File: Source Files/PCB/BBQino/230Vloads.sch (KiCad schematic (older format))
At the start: 3 parts

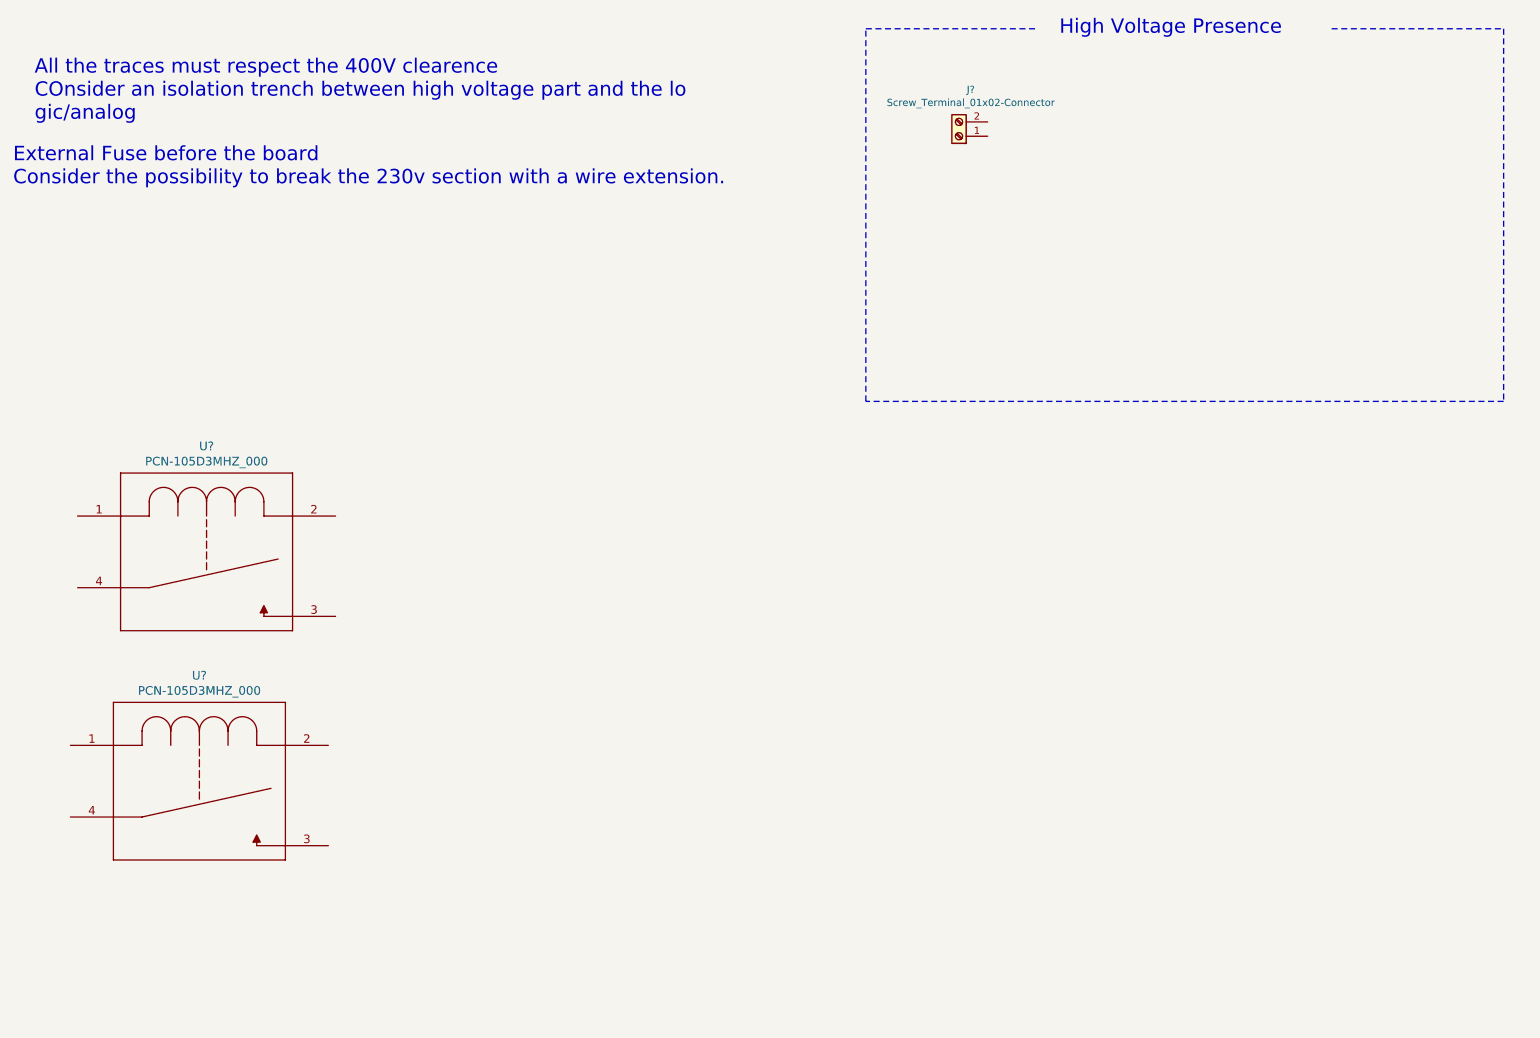
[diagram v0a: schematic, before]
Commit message: 230V section first Draft. Added external module on top of the shield for the 230V section
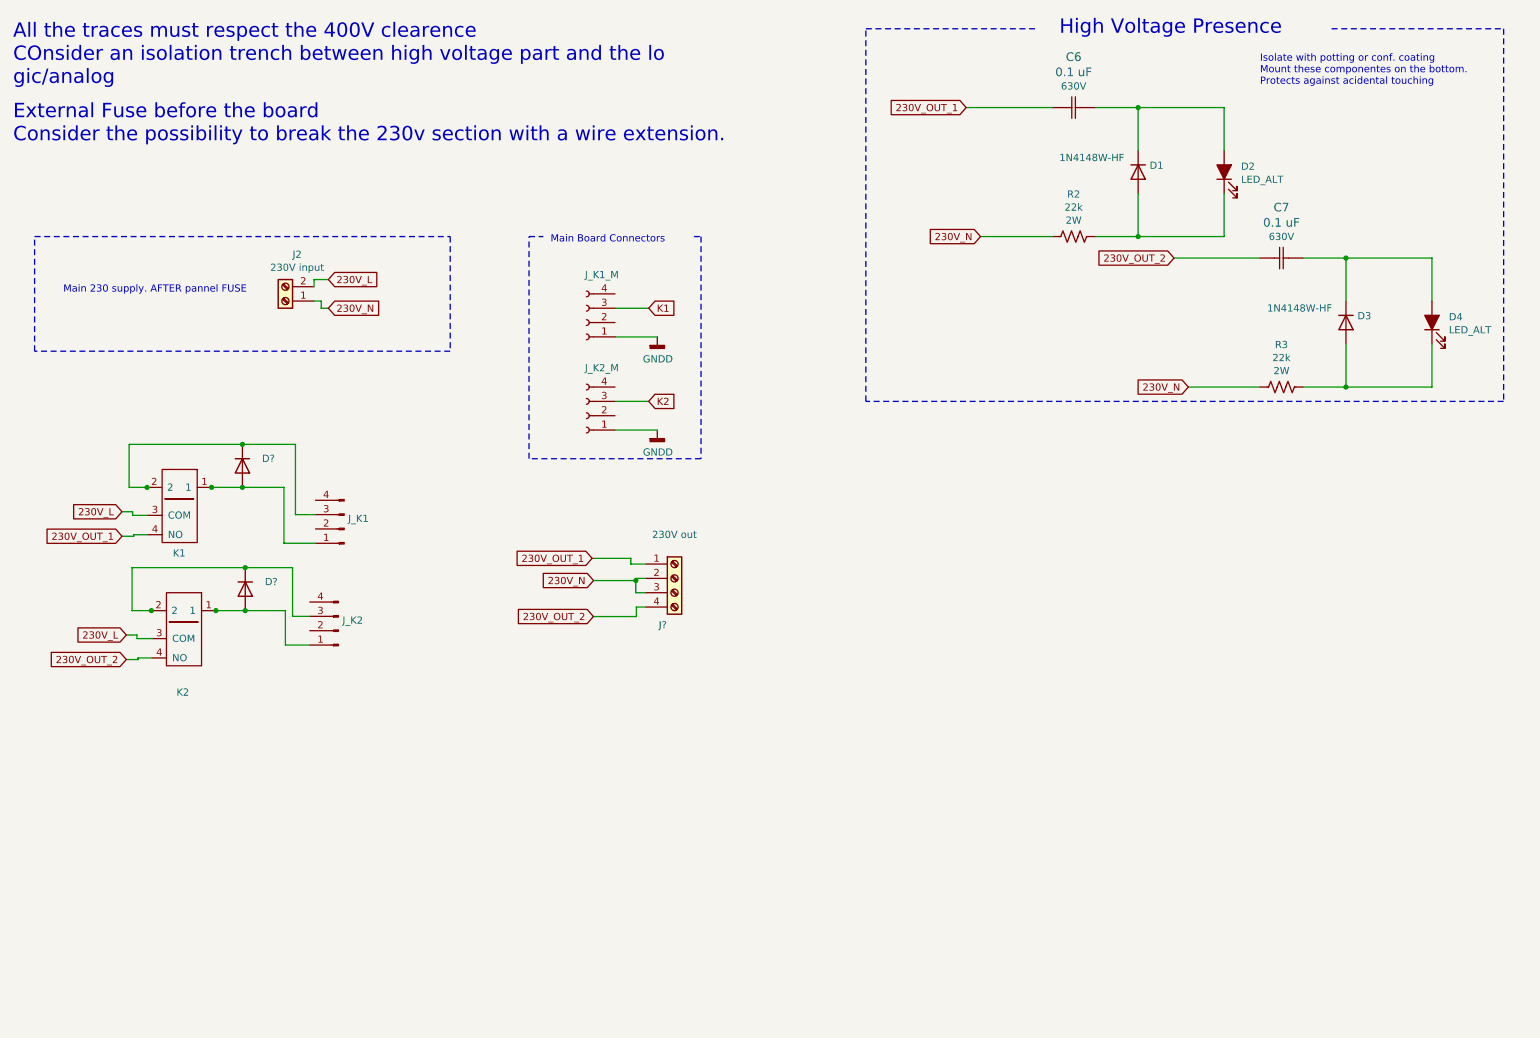
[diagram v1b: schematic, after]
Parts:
- removed U? (x2): PCN-105D3MHZ_000, RELAY_PCN-105D3MHZ_000_TYC, symbol BBQino-rescue:PCN-105D3MHZ_000
- added C6, C7: 0.1 uF, BBQino:ECWFE2J105K, symbol BBQino-rescue:ECWFE2J105K
- added D1, D3, D? (x2): 1N4148W-HF, Diode_SMD:D_SOD-123, symbol Diode:1N4007
- added D2, D4: LED_ALT, BBQino:150080BS75000, symbol Device:LED_ALT
- added J?: 230V out, Connector_TE-Connectivity:TE_826576-2_1x02_P3.96mm_Vertical, symbol Connector:Screw_Terminal_01x04
- added J_K1, J_K2: Conn_01x04_Male, symbol Connector:Conn_01x04_Male
- added J_K1_M, J_K2_M: Conn_01x04_Female, Connector_PinHeader_2.54mm:PinHeader_1x04_P2.54mm_Vertical, symbol Connector:Conn_01x04_Female
- added K1, K2: FTR-MYAA005D, BBQino:FTRMYAA005D, symbol BBQino-rescue:FTR-MYAA005D
- added R2, R3: 22k, Resistor_SMD:R_2010_5025Metric_Pad1.40x2.65mm_HandSolder, symbol Device:R_US
- J2: renamed from J?; value Screw_Terminal_01x02-Connector -> 230V input; footprint (none) -> Connector_TE-Connectivity:TE_826576-2_1x02_P3.96mm_Vertical
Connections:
- net labels added: 230V_L, 230V_N, 230V_OUT_1, 230V_OUT_2, GNDD, K1, K2
- wire segments 0 -> 76
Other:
- note added: "Isolate with potting or conf. coating \nMount these componentes on the bottom. \nProtects against acidental touching"
- note added: "Main 230 supply. AFTER pannel FUSE"
- note added: "Main Board Connectors"
- moved on the sheet: J2

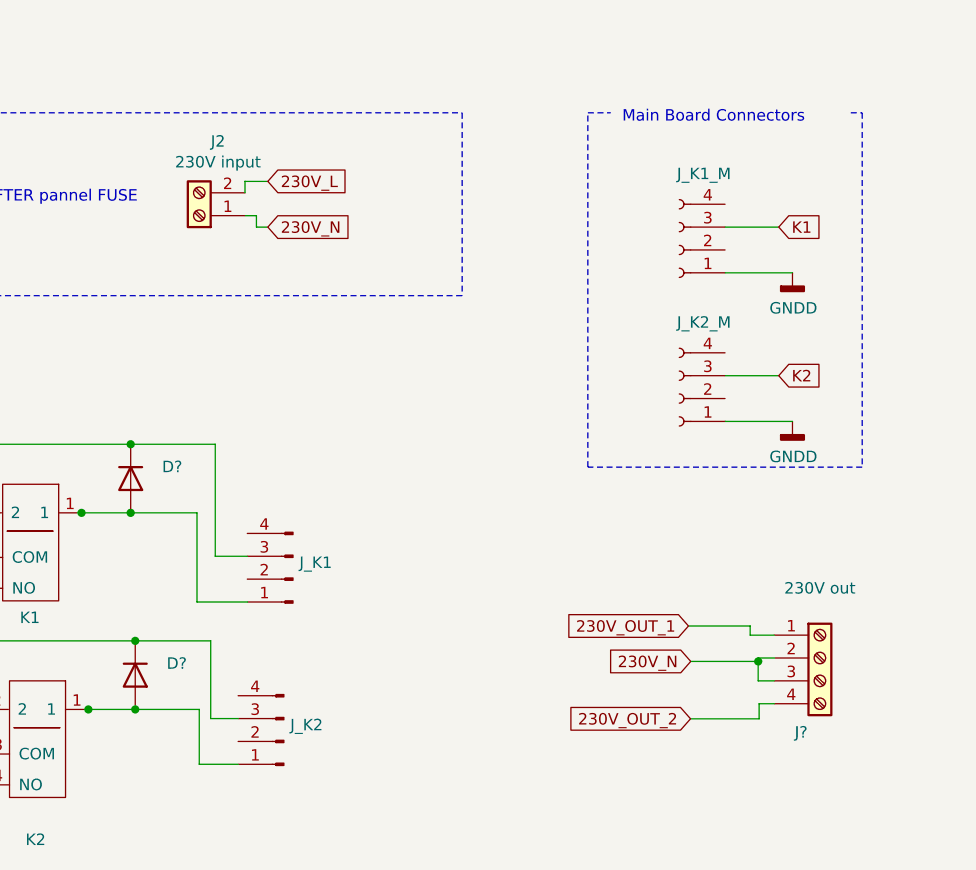
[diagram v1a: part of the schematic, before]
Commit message: Updated PCB external module
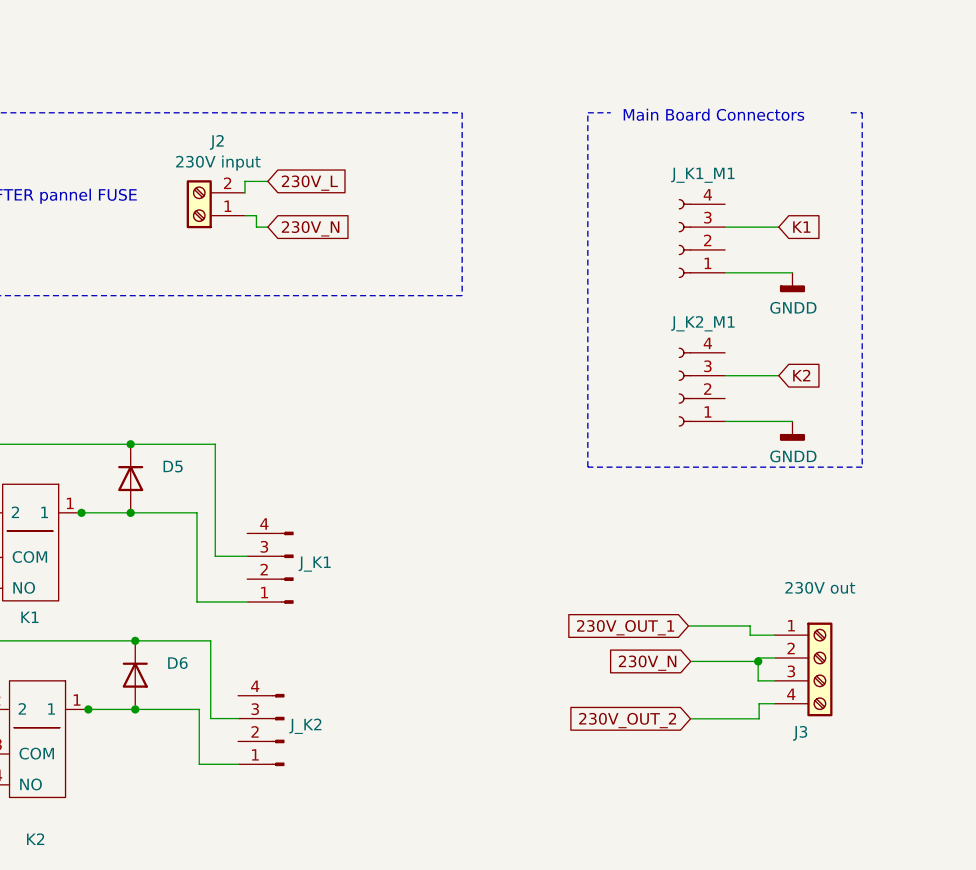
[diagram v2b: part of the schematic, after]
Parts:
- J3: renamed from J?; footprint Connector_TE-Connectivity:TE_826576-2_1x02_P3.96mm_Vertical -> BBQino:TB00250004BE
- gave numbers to parts that had none: 2
- renumbered J_K1_M to J_K1_M1, J_K2_M to J_K2_M1
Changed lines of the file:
@@
 Isolate with potting or conf. coating \nMount these componentes on the bottom. \nProtects against acidental touching
 $Comp
-L Connector:Conn_01x04_Female J_K1_M
+L Connector:Conn_01x04_Female J_K1_M1
 U 1 1 6151D7D1
 P 4600 2800
-F 0 "J_K1_M" H 4492 2467 50  0000 C CNN
+F 0 "J_K1_M1" H 4492 2467 50  0000 C CNN
 F 1 "Conn_01x04_Female" H 4492 2466 50  0001 C CNN
 F 2 "Connector_PinHeader_2.54mm:PinHeader_1x04_P2.54mm_Vertical" H 4600 2800 50  0001 C CNN
@@
 $EndComp
 $Comp
-L Connector:Conn_01x04_Female J_K2_M
+L Connector:Conn_01x04_Female J_K2_M1
 U 1 1 6151E93A
 P 4600 3450
-F 0 "J_K2_M" H 4492 3117 50  0000 C CNN
+F 0 "J_K2_M1" H 4492 3117 50  0000 C CNN
 F 1 "Conn_01x04_Female" H 4492 3116 50  0001 C CNN
 F 2 "Connector_PinHeader_2.54mm:PinHeader_1x04_P2.54mm_Vertical" H 4600 3450 50  0001 C CNN
@@
 K1
 $Comp
-L Diode:1N4007 D?
+L Diode:1N4007 D5
 U 1 1 6157CE68
 P 2200 3800
-F 0 "D?" V 2149 3937 50  0000 L CNN
+F 0 "D5" V 2149 3937 50  0000 L CNN
 F 1 "1N4148W-HF" H 1944 4032 50  0001 L CNN
 F 2 "Diode_SMD:D_SOD-123" H 2200 3625 50  0001 C CNN
@@
 $EndComp
 $Comp
-L Diode:1N4007 D?
+L Diode:1N4007 D6
 U 1 1 615877B5
 P 2220 4660
-F 0 "D?" V 2169 4797 50  0000 L CNN
+F 0 "D6" V 2169 4797 50  0000 L CNN
 F 1 "1N4148W-HF" H 1964 4892 50  0001 L CNN
 F 2 "Diode_SMD:D_SOD-123" H 2220 4485 50  0001 C CNN
@@
 	5035 3350 4800 3350
 $Comp
-L power:GNDD #PWR?
+L power:GNDD #PWR0114
 U 1 1 615A23E8
 P 5095 3550
-F 0 "#PWR?" H 5095 3300 50  0001 C CNN
+F 0 "#PWR0114" H 5095 3300 50  0001 C CNN
 F 1 "GNDD" H 5099 3395 50  0000 C CNN
 F 2 "" H 5095 3550 50  0001 C CNN
@@
 	4800 3550 5095 3550
 $Comp
-L power:GNDD #PWR?
+L power:GNDD #PWR0115
 U 1 1 615A714B
 P 5095 2900
-F 0 "#PWR?" H 5095 2650 50  0001 C CNN
+F 0 "#PWR0115" H 5095 2650 50  0001 C CNN
 F 1 "GNDD" H 5099 2745 50  0000 C CNN
 F 2 "" H 5095 2900 50  0001 C CNN
@@
 230V_N
 $Comp
-L Connector:Screw_Terminal_01x04 J?
+L Connector:Screw_Terminal_01x04 J3
 U 1 1 615B8777
 P 5215 4585
-F 0 "J?" H 5133 4260 50  0000 C CNN
+F 0 "J3" H 5133 4260 50  0000 C CNN
 F 1 "230V out" H 5215 4890 50  0000 C CNN
-F 2 "Connector_TE-Connectivity:TE_826576-2_1x02_P3.96mm_Vertical" H 5215 4585 50  0001 C CNN
-F 3 "" H 5215 4585 50  0001 C CNN
+F 2 "BBQino:TB00250004BE" H 5215 4585 50  0001 C CNN
+F 3 "https://www.mouser.it/datasheet/2/670/tb002_500-2306853.pdf" H 5215 4585 50  0001 C CNN
 	1    5215 4585
 	1    0    0    -1

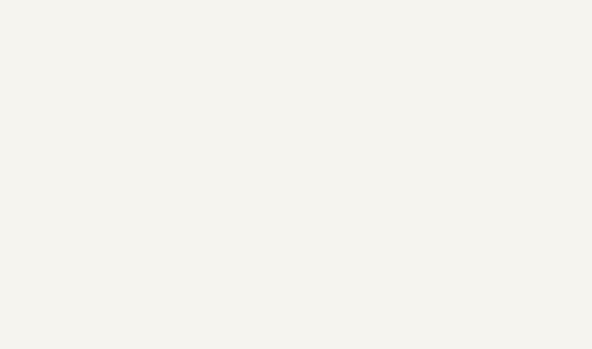
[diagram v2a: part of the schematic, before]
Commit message: added thermocouple interface
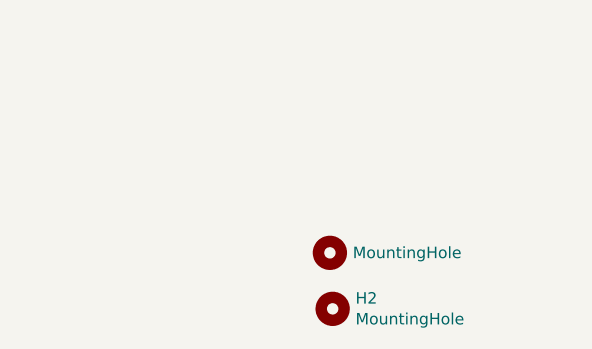
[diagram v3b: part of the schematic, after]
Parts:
- added H1, H2: MountingHole, MountingHole:MountingHole_3.5mm, symbol Mechanical:MountingHole
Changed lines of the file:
@@
 $Descr A4 11693 8268
 encoding utf-8
-Sheet 5 5
+Sheet 5 6
 Title ""
 Date ""
@@
 Wire Wire Line
 	4949 4785 5015 4785
+$Comp
+L Mechanical:MountingHole H1
+U 1 1 6151F1F6
+P 10108 5768
+F 0 "H1" H 10208 5814 50  0001 L CNN
+F 1 "MountingHole" H 10208 5768 50  0000 L CNN
+F 2 "MountingHole:MountingHole_3.5mm" H 10108 5768 50  0001 C CNN
+F 3 "~" H 10108 5768 50  0001 C CNN
+	1    10108 5768
+	1    0    0    -1
+$EndComp
+$Comp
+L Mechanical:MountingHole H2
+U 1 1 61520C2A
+P 10120 6013
+F 0 "H2" H 10220 6059 50  0000 L CNN
+F 1 "MountingHole" H 10220 5968 50  0000 L CNN
+F 2 "MountingHole:MountingHole_3.5mm" H 10120 6013 50  0001 C CNN
+F 3 "~" H 10120 6013 50  0001 C CNN
+	1    10120 6013
+	1    0    0    -1
+$EndComp
 $EndSCHEMATC

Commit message: updated schematic
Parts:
- added D7, D8: 1N4148W-HF, Diode_SMD:D_SOD-123, symbol Diode:1N4007
- added JP1: Jumper_2_Open, symbol Jumper:Jumper_2_Open
- added J_K11, J_K22: Conn_01x04_Male, symbol Connector:Conn_01x04_Male
- added K3, K4: FINDER-40.41, Relay_THT:Relay_SPDT_Finder_40.41, symbol Relay:FINDER-40.41
- added Q6, Q7: 2N7002K, Package_TO_SOT_SMD:SOT-23, symbol Transistor_FET:2N7002K
- added R12, R13: 100, symbol Device:R_US
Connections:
- net labels added: +12V, GNDPWR
- wire segments 76 -> 116
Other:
- note added: "5V relays\n"
- note added: "General purpose 12V relays"
